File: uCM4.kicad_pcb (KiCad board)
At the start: 2 copper layers, 55 x 40 mm, 30 parts, among them J1 Conn_01x03, J2 Ethernet, J3 Micro_SD_Card, J4 USB_B_Micro, SW1 SW_DIP_x01, SW2 SW_DIP_x01, U1 RT9742GGJ5, U2 74LVC1G07, U3 TPD4EUSB30

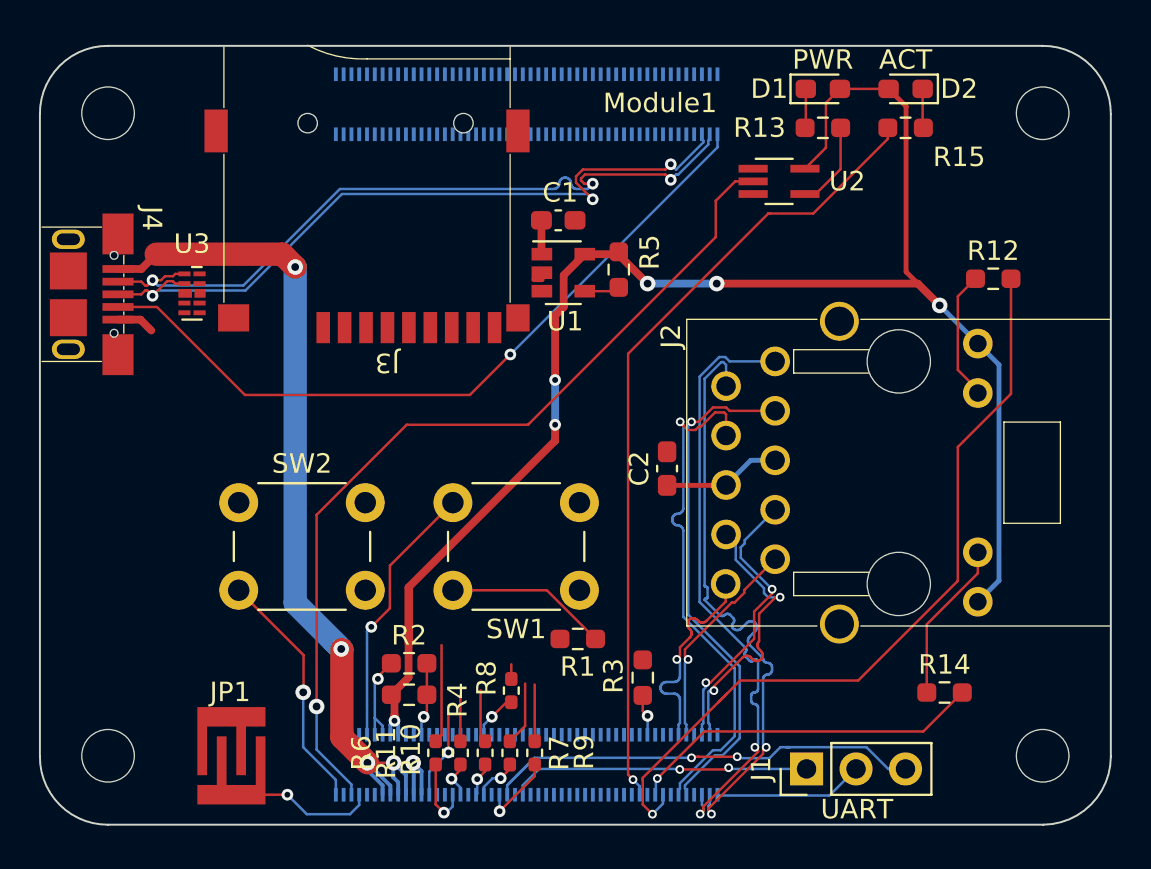
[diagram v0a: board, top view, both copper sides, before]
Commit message: Remove all routining beside main power rail
5V rail should be fine, as it keeps distance from faulty sections and
chances are Micro USB (and Hirose) will stay at their places.
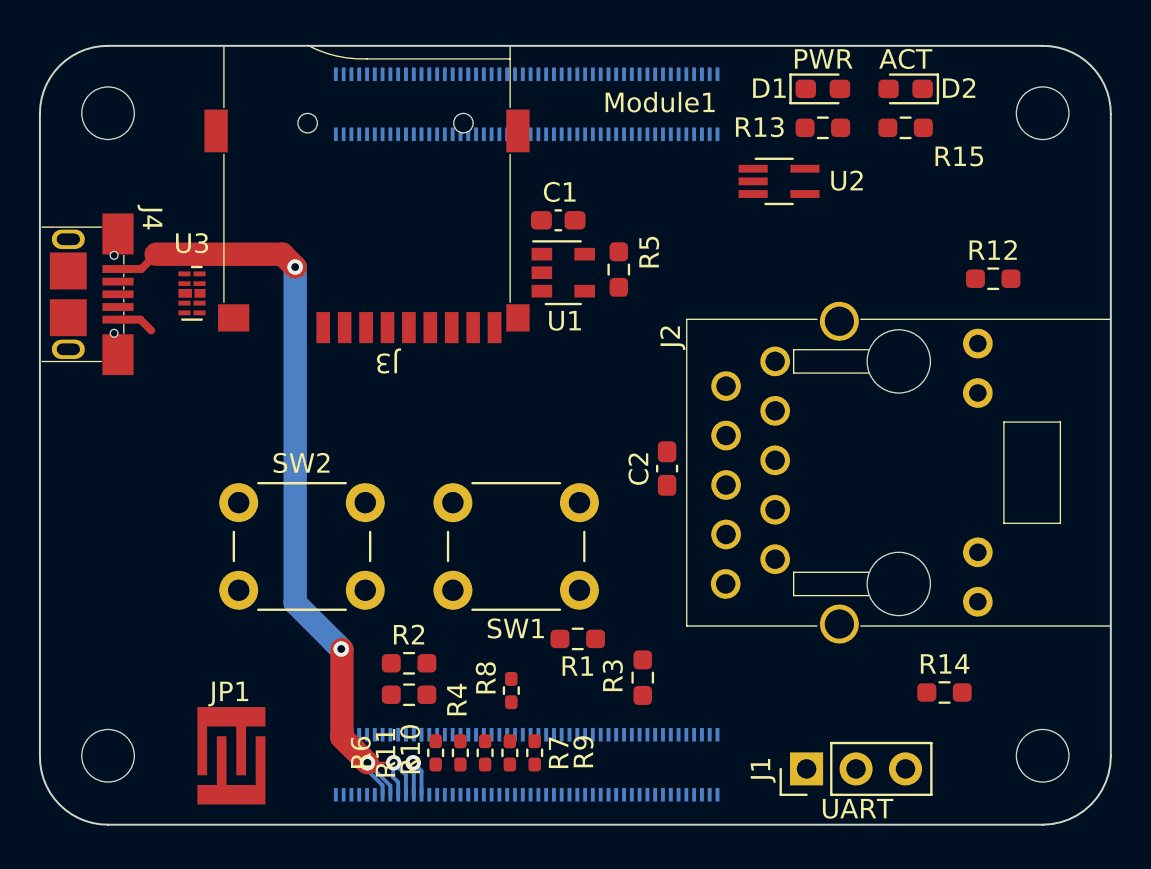
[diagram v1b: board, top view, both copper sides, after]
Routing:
- net +3V3: track 87.6 -> 0.00 mm, vias 6 -> 0
- net /nPWR_LED: track 45.8 -> 0.00 mm, vias 1 -> 0
- net Net-(Module1-Pad21): track 41.5 -> 0.00 mm, vias 1 -> 0
- net Net-(Module1-Pad15): track 40.9 -> 0.00 mm, vias 1 -> 0
- net Net-(J4-Pad4): track 38.6 -> 0.00 mm, vias 1 -> 0
- net /USB_P: track 38.3 -> 0.00 mm, vias 3 -> 0
- net /USB_N: track 38.1 -> 0.00 mm, vias 3 -> 0
- net /Eth_P3_N: track 31.3 -> 0.00 mm, vias 2 -> 0
- net /Eth_P3_P: track 31.3 -> 0.00 mm, vias 2 -> 0
- net /Eth_P2_P: track 26.4 -> 0.00 mm, vias 1 -> 0
- net /Eth_P2_N: track 26.4 -> 0.00 mm, vias 1 -> 0
- net /TX: track 24.1 -> 0.00 mm, vias 2 -> 0
- net Net-(Module1-Pad17): track 18.3 -> 0.00 mm, vias 1 -> 0
- net /RX: track 15.6 -> 0.00 mm, vias 2 -> 0
- net /Eth_P1_P: track 14.6 -> 0.00 mm, vias 2 -> 0
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
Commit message: Fix conflict of Micro SD and Hirose
Swap Micro SD with LEDs, move Ethernet downwards and fix positions of
most of minor components.
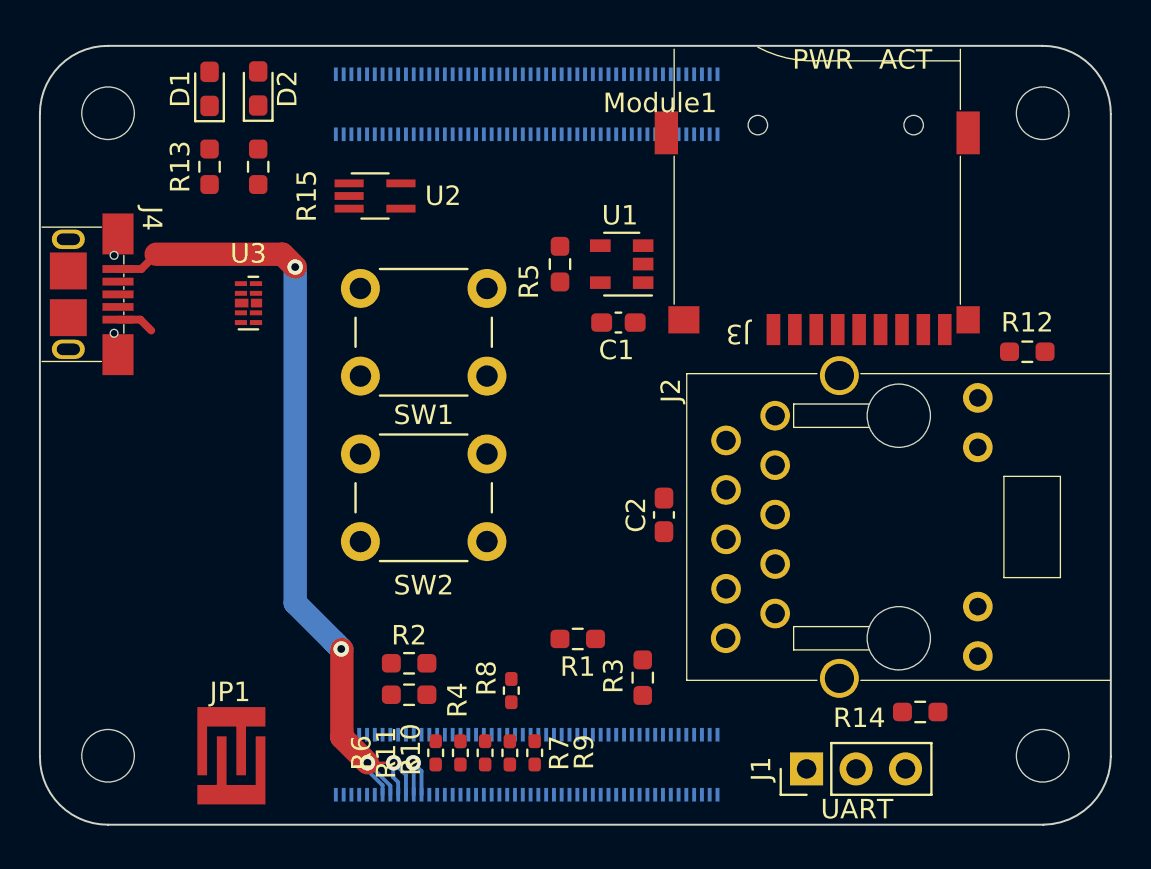
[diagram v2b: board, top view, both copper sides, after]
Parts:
- moved R15 33.3 mm to (149.0, 67.5), turned to 90 degrees
- moved D2 33.3 mm to (149.0, 63.5), turned to 90 degrees
- moved R13 31.6 mm to (146.5, 67.5), turned to -90 degrees
- moved D1 31.5 mm to (146.5, 63.5), turned to 90 degrees
- moved J3 23.1 mm to (177.7, 75.9)
- moved U2 20.8 mm to (155.0, 69.0)
- moved SW1 12.0 mm to (160.8, 78.2)
- moved SW2 6.73 mm to (154.2, 82.2)
- moved C1 6.09 mm to (167.5, 75.5), turned to 0 degrees
- moved R12 4.14 mm to (188.5, 77.0), turned to 180 degrees
- moved R5 3.03 mm to (164.5, 72.5), turned to -90 degrees
- moved U1 3.03 mm to (167.7, 72.5), turned to 180 degrees
- moved U3 2.94 mm to (148.5, 74.5)
- moved J2 2.79 mm to (181.9, 86.0)
- moved C2 2.39 mm to (169.8, 85.4)
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
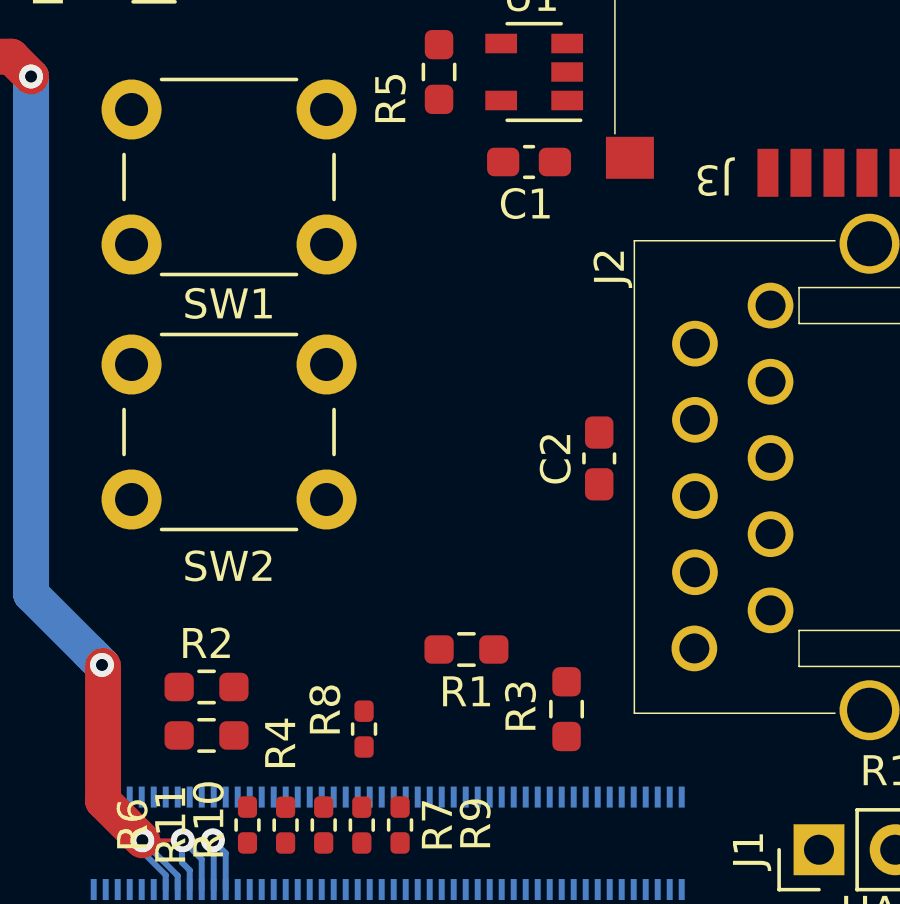
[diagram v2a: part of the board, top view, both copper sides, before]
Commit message: Remove notes from Eth connector
Remove all lines on User.Drawings layer that were used for designing and
checking the connector footprint.
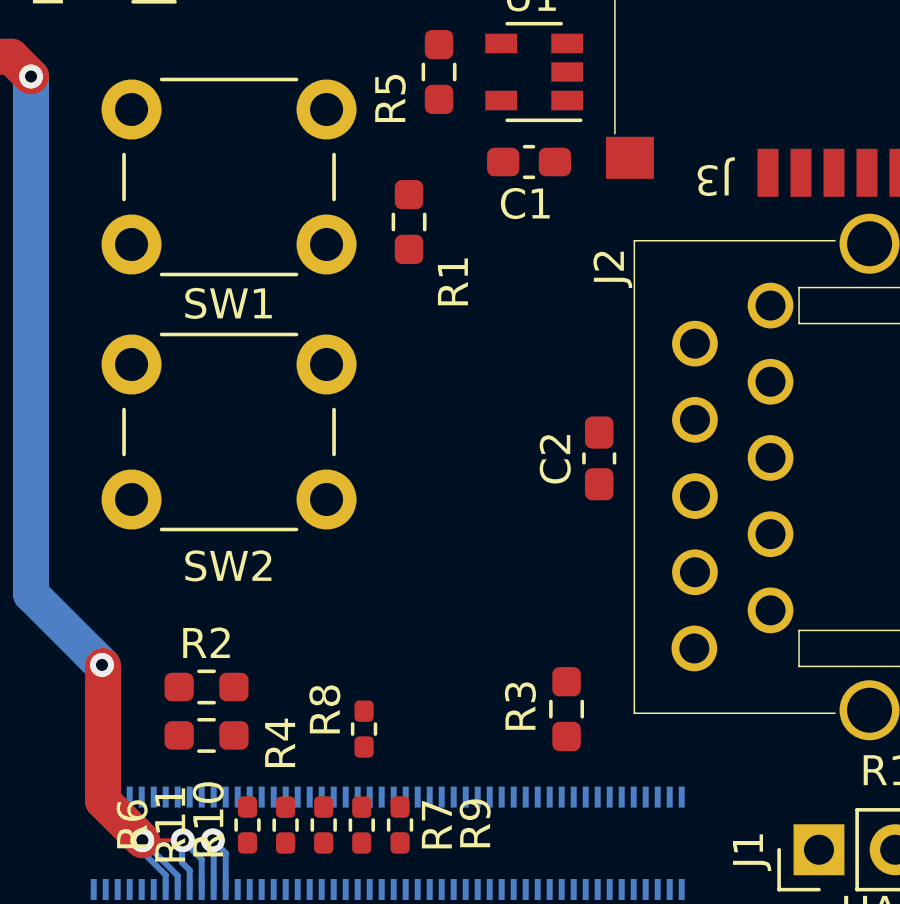
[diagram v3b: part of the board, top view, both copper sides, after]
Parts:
- moved R1 14.4 mm to (163.5, 77.5), turned to 90 degrees
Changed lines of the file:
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@@
       (effects (font (size 1 1) (thickness 0.15)))
     )
+    (fp_line (start -2.6 8.3) (end -2.6 5.4) (layer "F.SilkS") (width 0.05))
+    (fp_line (start -7.875 10.89) (end -7.875 -1.95) (layer "F.SilkS") (width 0.05))
+    (fp_line (start -5.115 -5.4) (end -5.115 -1.545) (layer "F.SilkS") (width 0.05))
+    (fp_line (start 5.115 -5.4) (end 6.315 -5.4) (layer "F.SilkS") (width 0.05))
+    (fp_line (start -2.6 5.4) (end 2.6 5.4) (layer "F.SilkS") (width 0.05))
+    (fp_line (start -7.875 -10.89) (end 7.875 -10.89) (layer "F.SilkS") (width 0.05))
+    (fp_line (start 7.875 10.89) (end 7.875 -1.95) (layer "F.SilkS") (width 0.05))
+    (fp_line (start 7.875 -4.2) (end 7.875 -10.89) (layer "F.SilkS") (width 0.05))
+    (fp_line (start 2.6 8.3) (end -2.6 8.3) (layer "F.SilkS") (width 0.05))
     (fp_line (start 5.115 -1.545) (end 5.115 -5.4) (layer "F.SilkS") (width 0.05))
-    (fp_line (start 7.875 10.89) (end 7.875 -1.95) (layer "F.SilkS") (width 0.05))
-    (fp_line (start -7.875 10.89) (end -7.875 -1.95) (layer "F.SilkS") (width 0.05))
-    (fp_line (start 2.6 8.3) (end -2.6 8.3) (layer "F.SilkS") (width 0.05))
-    (fp_line (start -2.6 5.4) (end 2.6 5.4) (layer "F.SilkS") (width 0.05))
+    (fp_line (start -7.875 -4.2) (end -7.875 -10.89) (layer "F.SilkS") (width 0.05))
+    (fp_line (start -6.315 -5.4) (end -5.115 -5.4) (layer "F.SilkS") (width 0.05))
+    (fp_line (start -6.315 -1.545) (end -6.315 -5.4) (layer "F.SilkS") (width 0.05))
+    (fp_line (start 2.6 5.4) (end 2.6 8.3) (layer "F.SilkS") (width 0.05))
     (fp_line (start 6.315 -5.4) (end 6.315 -1.545) (layer "F.SilkS") (width 0.05))
-    (fp_line (start 2.6 5.4) (end 2.6 8.3) (layer "F.SilkS") (width 0.05))
-    (fp_line (start -6.315 -1.545) (end -6.315 -5.4) (layer "F.SilkS") (width 0.05))
-    (fp_line (start -5.115 -5.4) (end -5.115 -1.545) (layer "F.SilkS") (width 0.05))
-    (fp_line (start -7.875 -4.2) (end -7.875 -10.89) (layer "F.SilkS") (width 0.05))
-    (fp_line (start -7.875 -10.89) (end 7.875 -10.89) (layer "F.SilkS") (width 0.05))
-    (fp_line (start -2.6 8.3) (end -2.6 5.4) (layer "F.SilkS") (width 0.05))
-    (fp_line (start 7.875 -4.2) (end 7.875 -10.89) (layer "F.SilkS") (width 0.05))
-    (fp_line (start -6.315 -5.4) (end -5.115 -5.4) (layer "F.SilkS") (width 0.05))
-    (fp_line (start 5.115 -5.4) (end 6.315 -5.4) (layer "F.SilkS") (width 0.05))
-    (fp_line (start -2.6 0) (end -2.6 5.4) (layer "Dwgs.User") (width 0.01))
-    (fp_line (start 1.905 -8.636) (end 4.445 -8.636) (layer "Dwgs.User") (width 0.05))
-    (fp_line (start -4.09 4.06) (end 0 4.06) (layer "Dwgs.User") (width 0.01))
-    (fp_line (start 0 4.06) (end -6.63 4.06) (layer "Dwgs.User") (width 0.01))
-    (fp_line (start -5.715 -0.12) (end -5.115 -0.12) (layer "Dwgs.User") (width 0.01))
-    (fp_line (start -5.715 -8.89) (end -5.715 -6.35) (layer "Dwgs.User") (width 0.05))
-    (fp_line (start -1.905 -6.35) (end 0.635 -6.35) (layer "Dwgs.User") (width 0.05))
-    (fp_line (start 0 4.59) (end -8.775 4.59) (layer "Dwgs.User") (width 0.01))
-    (fp_line (start 5.715 0) (end 5.715 10.89) (layer "Dwgs.User") (width 0.01))
-    (fp_line (start -5.715 0) (end -6.315 0) (layer "Dwgs.User") (width 0.01))
-    (fp_line (start 6.63 4.06) (end 0 4.06) (layer "Dwgs.User") (width 0.01))
-    (fp_line (start 0 -14.859) (end 0 11.99) (layer "Dwgs.User") (width 0.05))
-    (fp_line (start 5.715 0) (end -5.715 0) (layer "Dwgs.User") (width 0.05))
-    (fp_line (start -2.6 5.4) (end -2.6 8.3) (layer "Dwgs.User") (width 0.01))
-    (fp_line (start -7.875 10.89) (end -7.875 -10.89) (layer "Dwgs.User") (width 0.01))
-    (fp_line (start 5.715 -6.35) (end 5.715 0) (layer "Dwgs.User") (width 0.05))
-    (fp_line (start -8.775 0) (end -8.775 7.53) (layer "Dwgs.User") (width 0.01))
-    (fp_line (start 2.6 5.4) (end 2.6 8.3) (layer "Dwgs.User") (width 0.01))
-    (fp_line (start 5.715 -5.4) (end 5.115 -5.4) (layer "Dwgs.User") (width 0.01))
-    (fp_line (start 0 -3.05) (end -7.775 -3.05) (layer "Dwgs.User") (width 0.01))
-    (fp_line (start -5.715 -6.35) (end -4.445 -6.35) (layer "Dwgs.User") (width 0.05))
-    (fp_line (start 3.175 -6.35) (end 5.715 -6.35) (layer "Dwgs.User") (width 0.05))
-    (fp_line (start 8.775 7.03) (end 0 7.03) (layer "Dwgs.User") (width 0.01))
-    (fp_line (start -5.715 -5.4) (end -5.115 -5.4) (layer "Dwgs.User") (width 0.01))
-    (fp_line (start -4.41 0) (end -4.41 4.59) (layer "Dwgs.User") (width 0.01))
-    (fp_line (start -5.715 -10.287) (end 0 -10.287) (layer "Dwgs.User") (width 0.05))
-    (fp_line (start -5.715 0) (end -5.715 10.89) (layer "Dwgs.User") (width 0.01))
-    (fp_line (start 0 7.53) (end -8.775 7.53) (layer "Dwgs.User") (width 0.01))
-    (fp_line (start 0 5.4) (end 2.6 5.4) (layer "Dwgs.User") (width 0.01))
-    (fp_line (start 7.875 10.89) (end 7.875 -10.89) (layer "Dwgs.User") (width 0.01))
-    (fp_line (start 7.775 -3.05) (end 0 -3.05) (layer "Dwgs.User") (width 0.01))
-    (fp_line (start -4.445 -6.096) (end -1.905 -6.096) (layer "Dwgs.User") (width 0.05))
-    (fp_line (start -5.715 0) (end -5.715 -5.4) (layer "Dwgs.User") (width 0.01))
-    (fp_line (start 7.775 0) (end 7.775 -3.05) (layer "Dwgs.User") (width 0.01))
-    (fp_line (start -7.775 0) (end -7.775 -3.05) (layer "Dwgs.User") (width 0.01))
-    (fp_line (start -5.715 -5.4) (end -6.315 -5.4) (layer "Dwgs.User") (width 0.01))
-    (fp_line (start 0 4.06) (end 4.09 4.06) (layer "Dwgs.User") (width 0.01))
-    (fp_line (start -3.175 -8.636) (end -0.635 -8.636) (layer "Dwgs.User") (width 0.05))
-    (fp_line (start 5.715 0) (end 5.715 -5.4) (layer "Dwgs.User") (width 0.01))
-    (fp_line (start 0 5.4) (end -2.6 5.4) (layer "Dwgs.User") (width 0.01))
-    (fp_line (start -0.635 -8.89) (end 1.905 -8.89) (layer "Dwgs.User") (width 0.05))
-    (fp_line (start -5.715 -8.89) (end -3.175 -8.89) (layer "Dwgs.User") (width 0.05))
-    (fp_line (start 6.63 0) (end 6.63 4.06) (layer "Dwgs.User") (width 0.01))
-    (fp_line (start -7.875 10.89) (end 7.875 10.89) (layer "Dwgs.User") (width 0.01))
-    (fp_line (start 0.635 -6.096) (end 3.175 -6.096) (layer "Dwgs.User") (width 0.05))
-    (fp_line (start 2.6 0) (end 2.6 5.4) (layer "Dwgs.User") (width 0.01))
     (fp_line (start -7.875 10.89) (end 7.875 10.89) (layer "F.Fab") (width 0.1))
     (pad "" np_thru_hole circle (at -5.715 0 90) (locked) (size 3.25 3.25) (drill 3.25) (layers F&B.Cu *.Mask))
@@
       (polygon
         (pts
-          (xy 190.2 83.4)
-          (xy 190.2 88.6)
-          (xy 187.3 88.6)
-          (xy 187.3 83.4)
-        )
-      )
-    )
-    (zone (net 0) (net_name "") (layer "F.Cu") (hatch edge 0.508)
-      (connect_pads (clearance 0))
-      (min_thickness 0.254)
-      (keepout (tracks not_allowed) (vias not_allowed) (pads not_allowed ) (copperpour allowed) (footprints allowed))
-      (fill (thermal_gap 0.508) (thermal_bridge_width 0.508))
-      (polygon
-        (pts
           (xy 180.26 91.115)
           (xy 180.26 92.315)
@@
           (xy 176.5 80.885)
           (xy 176.5 79.685)
+        )
+      )
+    )
+    (zone (net 0) (net_name "") (layer "F.Cu") (hatch edge 0.508)
+      (connect_pads (clearance 0))
+      (min_thickness 0.254)
+      (keepout (tracks not_allowed) (vias not_allowed) (pads not_allowed ) (copperpour allowed) (footprints allowed))
+      (fill (thermal_gap 0.508) (thermal_bridge_width 0.508))
+      (polygon
+        (pts
+          (xy 190.2 83.4)
+          (xy 190.2 88.6)
+          (xy 187.3 88.6)
+          (xy 187.3 83.4)
         )
       )
@@
   )
   (footprint "Resistor_SMD:R_0603_1608Metric_Pad0.98x0.95mm_HandSolder" (layer "F.Cu")
-    (at 165.4125 91.75 180)
+    (at 163.5 77.5 90)
     (descr "Resistor SMD 0603 (1608 Metric), square (rectangular) end terminal, IPC_7351 nominal with elongated pad for handsoldering. (Body size source: IPC-SM-782 page 72, https://www.pcb-3d.com/wordpress/wp-content/uploads/ipc-sm-782a_amendment_1_and_2.pdf), generated with kicad-footprint-generator")
     (tags "resistor handsolder")
@@
     (property "Sheetname" "")
     (attr smd)
-    (fp_text reference "R1" (at 0 -1.43) (layer "F.SilkS")
-      (effects (font (size 1 1) (thickness 0.15)))
-    )
-    (fp_text value "220" (at 0 1.43) (layer "F.Fab")
-      (effects (font (size 1 1) (thickness 0.15)))
-    )
-    (fp_text user "${REFERENCE}" (at 0 0) (layer "F.Fab")
+    (fp_text reference "R1" (at -2 1.5 90) (layer "F.SilkS")
+      (effects (font (size 1 1) (thickness 0.15)))
+    )
+    (fp_text value "220" (at 0.5 2 90) (layer "F.Fab")
+      (effects (font (size 1 1) (thickness 0.15)))
+    )
+    (fp_text user "${REFERENCE}" (at 0 0 90) (layer "F.Fab")
       (effects (font (size 0.4 0.4) (thickness 0.06)))
     )
@@
     (fp_line (start 0.8 0.4125) (end -0.8 0.4125) (layer "F.Fab") (width 0.1))
     (fp_line (start -0.8 -0.4125) (end 0.8 -0.4125) (layer "F.Fab") (width 0.1))
-    (pad "1" smd roundrect (at -0.9125 0 180) (locked) (size 0.975 0.95) (layers "F.Cu" "F.Paste" "F.Mask") (roundrect_rratio 0.25)
+    (pad "1" smd roundrect (at -0.9125 0 90) (locked) (size 0.975 0.95) (layers "F.Cu" "F.Paste" "F.Mask") (roundrect_rratio 0.25)
       (net 116 "Net-(R1-Pad1)"))
-    (pad "2" smd roundrect (at 0.9125 0 180) (locked) (size 0.975 0.95) (layers "F.Cu" "F.Paste" "F.Mask") (roundrect_rratio 0.25)
+    (pad "2" smd roundrect (at 0.9125 0 90) (locked) (size 0.975 0.95) (layers "F.Cu" "F.Paste" "F.Mask") (roundrect_rratio 0.25)
       (net 4 "GND"))
     (model "${KISYS3DMOD}/Resistor_SMD.3dshapes/R_0603_1608Metric.wrl"
